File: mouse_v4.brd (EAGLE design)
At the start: 100 x 65 mm, 71 parts, among them U2 DRV8835DSSR

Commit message: v4 pre-polygon
Moved H-Bridge closer
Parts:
- removed C_V1, C_V2, C_V4: 0.1uF, SparkFun:0603-CAP
- removed C_V5: 4.7uF, SparkFun:0603-CAP
- removed V_CAP2: 2.2uF, SparkFun:0603-CAP
- added C_VA1, C_VDD1, C_VDD2: 0.1uF, SparkFun:0603-CAP
- added C_VA2: 4.7uF, SparkFun:0603-CAP
- added V_VCAP1: 2.2uF, SparkFun:0603-CAP
- R_BOOT0, R_BOOT1, R_NRST: device rcl:0204V -> SparkFun-Resistors:0603-RES
- moved R_BOOT1 331.3 mm to (76.5, 35.0), turned to 180 degrees
- moved C_VBAT 328.5 mm to (61.7, 26.4), turned to 180 degrees
- moved LED2 327.6 mm to (17.7, 3.35), turned to 180 degrees
- moved LED1 325.5 mm to (19.6, 3.35), turned to 180 degrees
- moved C_V0 322.1 mm to (74.9, 29.6), turned to 90 degrees
- moved C_VCAP2 321.7 mm to (63.6, 42.2), turned to 270 degrees
- moved U$8 306.7 mm to (23.7, 28.8)
- moved R_NRST 299.6 mm to (3.00, 16.0), turned to 90 degrees
- moved R_LED3 292.1 mm to (14.4, 6.42), turned to 90 degrees
- moved R_LED2 291.7 mm to (17.7, 6.48), turned to 90 degrees
- moved R_LED1 290.8 mm to (19.7, 6.54), turned to 90 degrees
- moved LED3 290.1 mm to (14.2, 3.35), turned to 180 degrees
- moved R_BOOT0 285.4 mm to (4.00, 20.0), turned to 180 degrees
- moved NRST_SWITCH 258.8 mm to (5.19, 8.63), turned to 270 degrees
- moved C_HB-BAT 241.7 mm to (22.6, 31.8)
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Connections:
- removed net 3.3V: GYRO.1, GYRO.10, GYRO.5, GYRO.9, PIN_HEADERS.1
- removed net 3V3_NUCLEO: JP1.6, JP1.7, U$4.C, U$5.C, U$6.C, U$7.C
- removed net AGND: C_V4.2, C_V5.2, U$1.VSSA
- removed net N$1: R_BOOT1.1
- net 3V3: now also C_VA1.1, C_VA2.1, C_VDD1.1, C_VDD2.2, GYRO.1, GYRO.10, GYRO.5, GYRO.9, JP1.6, JP1.7, PIN_HEADERS.1, U$4.C, U$5.C, U$6.C, U$7.C; no longer C_V1.1, C_V2.2, C_V4.1, C_V5.1
- net EMIT_FL: now also U$1.PB14; no longer U$1.PC11
- net EMIT_FR: now also U$1.PA2; no longer U$1.PB0
- net EMIT_L: now also U$1.PB15; no longer U$1.PC10
- net EMIT_R: now also U$1.PC1; no longer U$1.PB7
- net ENC_A2: now also U$1.PB4; no longer U$1.PA1
- net ENC_B2: now also U$1.PB5; no longer U$1.PA3
- net GND: now also C_VA1.2, C_VA2.2, C_VDD1.2, C_VDD2.1, R_BOOT1.1, U$1.VSSA, V_VCAP1.1; no longer C_V1.2, C_V2.1, V_CAP2.1
- net HB_B1: now also U$1.PB7; no longer U$1.PB10
- net HB_B2: now also U$1.PB9; no longer U$1.PB6
- net HB_F1: now also U$1.PB6; no longer U$1.PC7
- net HB_F2: now also U$1.PB8; no longer U$1.PA7
- net HB_MODE: now also U$1.PC11; no longer U$1.PC9
- net LED1: now also U$1.PC15; no longer U$1.PB12
- net LED2: now also U$1.PC14; no longer U$1.PB13
- net N$4: now also V_VCAP1.2; no longer V_CAP2.2
- net REC_FL: now also U$1.PB1; no longer U$1.PA4
- net REC_FR: now also U$1.PA6; no longer U$1.PC1
- net REC_L: now also U$1.PB0; no longer U$1.PA0_WKUP
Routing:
- net GND: track 0.00 -> 522.3 mm, vias 0 -> 12
- net 3V3: track 0.00 -> 364.5 mm, vias 0 -> 8
- net 5V: track 0.00 -> 241.9 mm, vias 0 -> 5
- net NRST: track 0.00 -> 128.8 mm
- net BOOT0: track 0.00 -> 68.0 mm, vias 0 -> 2
- net BAT: track 0.00 -> 62.2 mm, vias 0 -> 3
- net LED2: track 0.00 -> 58.3 mm
- net LED1: track 0.00 -> 56.8 mm
- net REC_R: track 0.00 -> 43.3 mm
- net REC_L: track 0.00 -> 40.7 mm
- net HB_B2: track 0.00 -> 40.1 mm
- net HB_F2: track 0.00 -> 39.4 mm
- net HB_B1: track 0.00 -> 37.7 mm
- net HB_MODE: track 0.00 -> 36.7 mm, vias 0 -> 2
- net HB_F1: track 0.00 -> 36.5 mm
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- added copper zone on layer 1, net MGND
- removed copper zone on layer 16, net GND

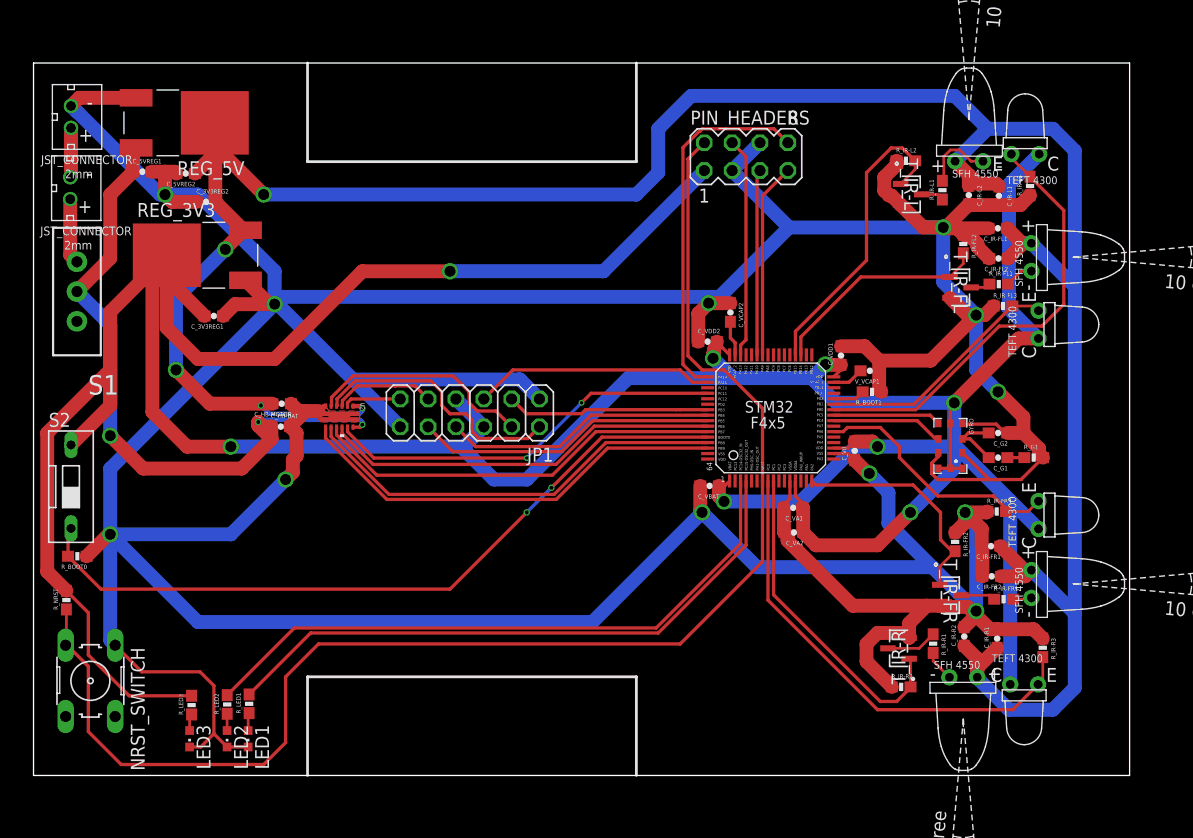
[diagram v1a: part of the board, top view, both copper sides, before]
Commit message: Changed H-Bridge + Holes
Changed the H-bridge smd layout and added holes for the wheel mounts
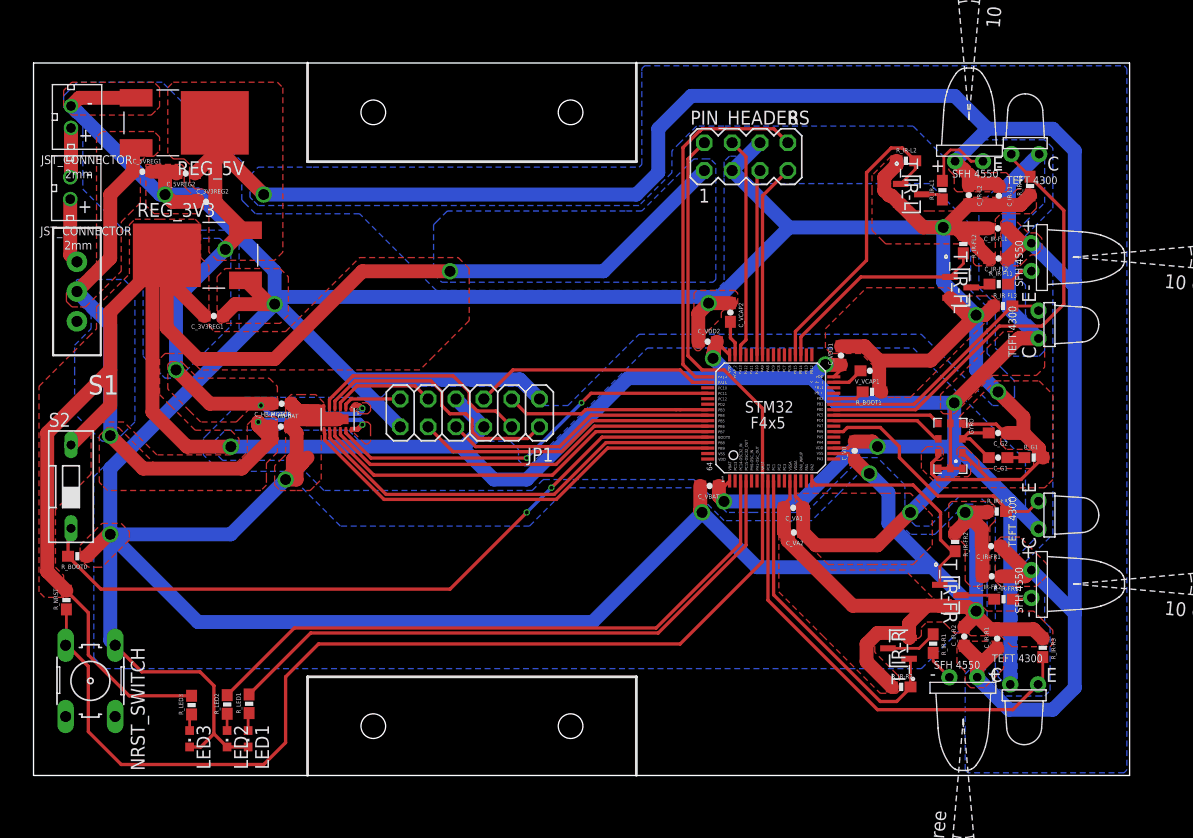
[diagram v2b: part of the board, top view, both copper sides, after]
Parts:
- removed U2: DRV8835DSSR, DRV8835:DSS12_P9X2
- added U$9: DRV8835, DRV8835:12-WFDFN
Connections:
- net 5V: now also U$9.1; no longer U2.1
- net BAT: now also U$9.12; no longer U2.12
- net HB_B1: now also U$9.9; no longer U2.9
- net HB_B2: now also U$9.7; no longer U2.7
- net HB_F1: now also U$9.10; no longer U2.10
- net HB_F2: now also U$9.8; no longer U2.8
- net HB_MODE: now also U$9.11; no longer U2.11
- net MGND: now also U$9.13, U$9.6; no longer U2.13, U2.6
- net M_B1: now also U$9.3; no longer U2.3
- net M_B2: now also U$9.5; no longer U2.5
- net M_F1: now also U$9.2; no longer U2.2
- net M_F2: now also U$9.4; no longer U2.4
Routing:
- net MGND: track 7.27 -> 15.8 mm
- net GND: track 522.3 -> 525.7 mm
- added copper zone on layer 1, net 3V3
- added copper zone on layer 16, net 3V3
- added copper zone on layer 1, net 5V
- added copper zone on layer 16, net 5V
- added copper zone on layer 1, net BAT
- added copper zone on layer 16, net BAT
- added copper zone on layer 1, net GND
- added copper zone on layer 16, net GND
- added copper zone on layer 16, net N$1

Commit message: polygon attempt pt2
Removed all the small polygons and added a huge GND polygon on the bototm. Unsure what to do for the power polygons on top
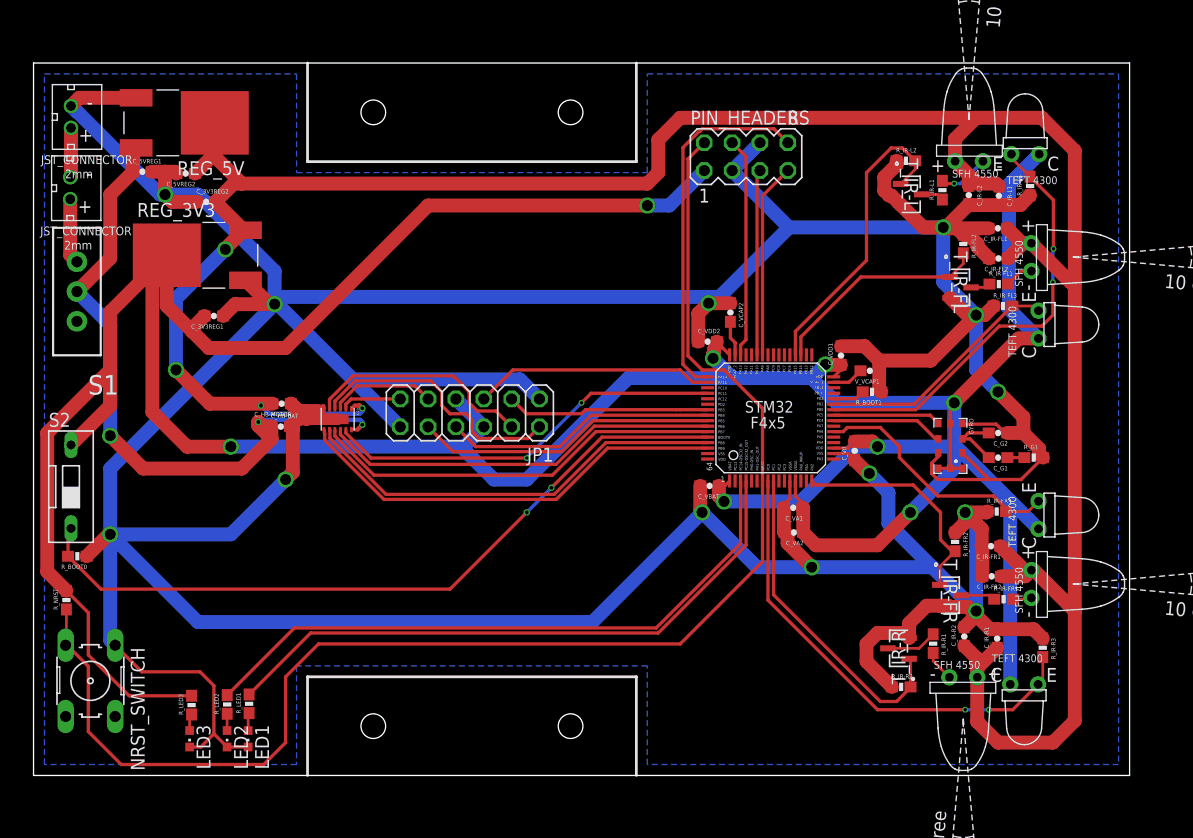
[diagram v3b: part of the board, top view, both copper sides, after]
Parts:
- moved U$8 1.50 mm to (23.7, 30.3)
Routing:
- net GND: track 525.7 -> 510.7 mm, vias 12 -> 13
- net 3V3: track 364.5 -> 359.5 mm
- net 5V: track 242.2 -> 245.0 mm, vias 5 -> 4
- net N$24: track 6.52 -> 4.65 mm, vias 0 -> 1
- net REC_L: track 40.7 -> 40.1 mm, vias 0 -> 2
- net REC_R: vias 0 -> 2
- removed copper zone on layer 1, net 3V3
- removed copper zone on layer 16, net 3V3
- removed copper zone on layer 1, net 5V
- removed copper zone on layer 16, net 5V
- removed copper zone on layer 1, net BAT
- removed copper zone on layer 16, net BAT
- removed copper zone on layer 1, net GND
- removed copper zone on layer 1, net MGND
- removed copper zone on layer 16, net N$1

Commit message: Changed IR LED Resistors
Switched voltage from 5V to 3.3V for IR LEDs, and changed resistor values accordingly
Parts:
- R_IR-FL1, R_IR-FR1, R_IR-L1, R_IR-R1: value 51 -> 15
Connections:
- net 3V3: now also C_IR-FL1.1, C_IR-FL2.1, C_IR-FR1.1, C_IR-FR2.1, C_IR-L1.1, C_IR-L2.1, C_IR-R1.1, C_IR-R2.1, IR_FL.+, IR_FR.+, IR_L.+, IR_R.+
- net 5V: no longer C_IR-FL1.1, C_IR-FL2.1, C_IR-FR1.1, C_IR-FR2.1, C_IR-L1.1, C_IR-L2.1, C_IR-R1.1, C_IR-R2.1, IR_FL.+, IR_FR.+, IR_L.+, IR_R.+
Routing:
- net 5V: track 245.0 -> 209.4 mm
- net 3V3: track 359.5 -> 383.7 mm

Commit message: Added power plane
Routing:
- net 5V: track 209.4 -> 50.7 mm
- added copper zone on layer 1, net 3V3
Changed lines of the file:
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@@
 <?xml version="1.0" encoding="utf-8"?>
 <!DOCTYPE eagle SYSTEM "eagle.dtd">
-<eagle version="9.2.2">
+<eagle version="8.6.1">
 <drawing>
 <settings>
@@
 <grid distance="1" unitdist="mm" unit="mm" style="lines" multiple="1" display="yes" altdistance="0.25" altunitdist="mm" altunit="mm"/>
 <layers>
-<layer number="1" name="Top" color="4" fill="1" visible="yes" active="yes"/>
+<layer number="1" name="Top" color="4" fill="1" visible="no" active="yes"/>
 <layer number="16" name="Bottom" color="1" fill="1" visible="yes" active="yes"/>
 <layer number="17" name="Pads" color="2" fill="1" visible="yes" active="yes"/>
@@
 <param name="checkStop" value="0"/>
 <param name="checkValues" value="0"/>
-<param name="checkNames" value="1"/>
-<param name="checkWireStubs" value="1"/>
-<param name="checkPolygonWidth" value="0"/>
 <param name="useDiameter" value="13"/>
 <param name="maxErrors" value="50"/>
@@
 <wire x1="29.75" y1="33.75" x2="30" y2="33.5" width="0.4064" layer="1"/>
 <wire x1="29.3" y1="33.75" x2="29.75" y2="33.75" width="0.4064" layer="1"/>
-<wire x1="86.1" y1="4.9" x2="88" y2="3" width="1.27" layer="1"/>
-<wire x1="93" y1="3" x2="95" y2="5" width="1.27" layer="1"/>
-<wire x1="95" y1="5" x2="95" y2="15" width="1.27" layer="1"/>
-<wire x1="95" y1="15" x2="91.26" y2="18.74" width="1.27" layer="1"/>
-<wire x1="88" y1="3" x2="93" y2="3" width="1.27" layer="1"/>
-<wire x1="95" y1="45" x2="95" y2="15" width="1.27" layer="1"/>
-<wire x1="94.6" y1="45" x2="95" y2="45" width="1.27" layer="1"/>
-<wire x1="95" y1="45" x2="95" y2="57" width="1.27" layer="1"/>
-<wire x1="95" y1="57" x2="92" y2="60" width="1.27" layer="1"/>
-<wire x1="92" y1="60" x2="86" y2="60" width="1.27" layer="1"/>
-<wire x1="86" y1="60" x2="59" y2="60" width="1.27" layer="1"/>
-<wire x1="59" y1="60" x2="57" y2="58" width="1.27" layer="1"/>
-<wire x1="57" y1="58" x2="57" y2="55" width="1.27" layer="1"/>
-<wire x1="84.08" y1="58.08" x2="86" y2="60" width="1.27" layer="1"/>
-<wire x1="57" y1="55" x2="56" y2="54" width="1.27" layer="1"/>
-<wire x1="18.26" y1="54" x2="16.59" y2="52.33" width="1.27" layer="1"/>
-<wire x1="56" y1="54" x2="19" y2="54" width="1.27" layer="1"/>
-<wire x1="19" y1="54" x2="18.26" y2="54" width="1.27" layer="1"/>
-<wire x1="16.54" y1="59.54" x2="16.54" y2="56.46" width="1.27" layer="1"/>
-<wire x1="16.54" y1="56.46" x2="19" y2="54" width="1.27" layer="1"/>
+<wire x1="14.73" y1="54.92" x2="16.59" y2="53.06" width="1.27" layer="1"/>
+<wire x1="16.59" y1="53.06" x2="16.59" y2="52.33" width="1.27" layer="1"/>
 </signal>
 <signal name="N$2">
@@
 <wire x1="86.12" y1="54" x2="85.33" y2="54.79" width="1.27" layer="1"/>
 <wire x1="87.82" y1="54" x2="86.12" y2="54" width="1.27" layer="1"/>
-<wire x1="89" y1="53.94" x2="88.08" y2="53.74" width="0" layer="19" extent="1-16"/>
-<wire x1="86.1" y1="8.96" x2="89.11" y2="8.31" width="0" layer="19" extent="1-1"/>
-<wire x1="91.04" y1="18.74" x2="91.69" y2="22.49" width="0" layer="19" extent="1-1"/>
-<wire x1="88.83" y1="49.92" x2="88.08" y2="53.74" width="0" layer="19" extent="1-1"/>
+<polygon width="0.1524" layer="1">
+<vertex x="1" y="64"/>
+<vertex x="24" y="64"/>
+<vertex x="24" y="55"/>
+<vertex x="56" y="55"/>
+<vertex x="56" y="64"/>
+<vertex x="99" y="64"/>
+<vertex x="99" y="1"/>
+<vertex x="56" y="1"/>
+<vertex x="56" y="10"/>
+<vertex x="24" y="10"/>
+<vertex x="24" y="1"/>
+<vertex x="1" y="1"/>
+</polygon>
 </signal>
 <signal name="BOOT0">
@@
 </signal>
 </signals>
-<mfgpreviewcolors>
-<mfgpreviewcolor name="soldermaskcolor" color="0xC8008000"/>
-<mfgpreviewcolor name="silkscreencolor" color="0xFFFEFEFE"/>
-<mfgpreviewcolor name="backgroundcolor" color="0xFF282828"/>
-<mfgpreviewcolor name="coppercolor" color="0xFFFFBF00"/>
-<mfgpreviewcolor name="substratecolor" color="0xFF786E46"/>
-</mfgpreviewcolors>
 </board>
 </drawing>
